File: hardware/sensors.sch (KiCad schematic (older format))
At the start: 31 parts, among them U1 LM358, U2 LAH-100P, U3 LOC110, U4 MCP6001, U5 ADA4805-1

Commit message: Draft layout of controller section
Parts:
- removed TH1, TH2: NXRT15WB473FA1B, symbol THERMISTOR
- added C73: 100n, Capacitors_SMD:C_0603, symbol C
- added C78: 1u, Capacitors_SMD:C_0603, symbol C
- added P13: CONN_01X02_MTMP, 2kwMotorController:TERM_2P_2-5_1990009, symbol CONN_01X02
- added P14: CONN_01X02_BTMP, 2kwMotorController:TERM_2P_2-5_1990009, symbol CONN_01X02
- R3: footprint Resistors_SMD:R_0603 -> Resistors_SMD:R_1206
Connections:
- wire segments 90 -> 94
- no-connect marks 0 -> 2
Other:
- note added: "NTC THERMISTOR\nPROBE OFF-BOARD:\nNXRT15WB473FA1B"
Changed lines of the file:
@@
 F 0 "R3" V 3180 2000 50  0000 C CNN
 F 1 "59.0" V 3100 2000 50  0000 C CNN
-F 2 "Resistors_SMD:R_0603" V 3030 2000 50  0001 C CNN
+F 2 "Resistors_SMD:R_1206" V 3030 2000 50  0001 C CNN
 F 3 "" H 3100 2000 50  0000 C CNN
 	1    3100 2000
@@
 L +12V #PWR04
 U 1 1 59A9BD78
-P 800 1550
-F 0 "#PWR04" H 800 1400 50  0001 C CNN
-F 1 "+12V" H 800 1690 50  0000 C CNN
-F 2 "" H 800 1550 50  0000 C CNN
-F 3 "" H 800 1550 50  0000 C CNN
-	1    800  1550
+P 950 1550
+F 0 "#PWR04" H 950 1400 50  0001 C CNN
+F 1 "+12V" H 950 1690 50  0000 C CNN
+F 2 "" H 950 1550 50  0000 C CNN
+F 3 "" H 950 1550 50  0000 C CNN
+	1    950  1550
 	1    0    0    -1
 $EndComp
@@
 L -12V #PWR2
 U 1 1 59A9BF35
-P 800 1750
-F 0 "#PWR2" H 800 1850 50  0001 C CNN
-F 1 "-12V" H 800 1900 50  0000 C CNN
-F 2 "" H 800 1750 50  0000 C CNN
-F 3 "" H 800 1750 50  0000 C CNN
-	1    800  1750
+P 950 2050
+F 0 "#PWR2" H 950 2150 50  0001 C CNN
+F 1 "-12V" H 950 2200 50  0000 C CNN
+F 2 "" H 950 2050 50  0000 C CNN
+F 3 "" H 950 2050 50  0000 C CNN
+	1    950  2050
 	-1   0    0    1
 $EndComp
@@
 	1650 1450 1600 1450
 Wire Wire Line
-	800  1600 1650 1600
-Wire Wire Line
-	800  1700 1650 1700
+	950  1600 1650 1600
 Wire Wire Line
 	2650 1650 3100 1650
@@
 Connection ~ 3500 6750
 Wire Wire Line
-	800  1600 800  1550
-Wire Wire Line
-	800  1750 800  1700
+	950  1550 950  1650
 Wire Wire Line
 	2650 1450 2700 1450
@@
 Connection ~ 5000 6650
 $Comp
-L THERMISTOR TH1
-U 1 1 59BEC427
-P 8300 2400
-F 0 "TH1" V 8400 2450 50  0000 C CNN
-F 1 "NXRT15WB473FA1B" V 8200 2400 50  0000 C BNN
-F 2 "" H 8300 2400 50  0001 C CNN
-F 3 "" H 8300 2400 50  0000 C CNN
-	1    8300 2400
-	1    0    0    -1
-$EndComp
-$Comp
 L R R38
 U 1 1 59BEC59E
@@
 $EndComp
 Wire Wire Line
-	8300 2700 8300 2650
-Wire Wire Line
-	8300 2050 8300 2150
+	8300 2450 8300 2700
+Wire Wire Line
+	8300 2050 8300 2350
 Wire Wire Line
 	8300 1750 8300 1650
@@
 $EndComp
 $Comp
-L THERMISTOR TH2
-U 1 1 59C18B62
-P 8300 4850
-F 0 "TH2" V 8400 4900 50  0000 C CNN
-F 1 "NXRT15WB473FA1B" V 8200 4850 50  0000 C BNN
-F 2 "" H 8300 4850 50  0001 C CNN
-F 3 "" H 8300 4850 50  0000 C CNN
-	1    8300 4850
-	1    0    0    -1
-$EndComp
-$Comp
 L R R59
 U 1 1 59C18B68
@@
 $EndComp
 Wire Wire Line
-	8300 5150 8300 5100
-Wire Wire Line
-	8300 4500 8300 4600
+	8300 4900 8300 5150
+Wire Wire Line
+	8300 4500 8300 4800
 Wire Wire Line
 	8300 4200 8300 4100
@@
 Connection ~ 2700 4650
 Connection ~ 2700 4250
+NoConn ~ 4100 1400
+NoConn ~ 4750 6050
+$Comp
+L C C73
+U 1 1 59CB7B98
+P 950 1800
+F 0 "C73" H 975 1900 50  0000 L CNN
+F 1 "100n" H 975 1700 50  0000 L CNN
+F 2 "Capacitors_SMD:C_0603" H 988 1650 50  0001 C CNN
+F 3 "" H 950 1800 50  0000 C CNN
+	1    950  1800
+	1    0    0    -1
+$EndComp
+Connection ~ 950  1600
+Wire Wire Line
+	950  1950 950  2050
+Wire Wire Line
+	950  2000 1550 2000
+Wire Wire Line
+	1550 2000 1550 1700
+Wire Wire Line
+	1550 1700 1650 1700
+Connection ~ 950  2000
+$Comp
+L C C78
+U 1 1 59CB93D8
+P 1250 1800
+F 0 "C78" H 1275 1900 50  0000 L CNN
+F 1 "1u" H 1275 1700 50  0000 L CNN
+F 2 "Capacitors_SMD:C_0603" H 1288 1650 50  0001 C CNN
+F 3 "" H 1250 1800 50  0000 C CNN
+	1    1250 1800
+	1    0    0    -1
+$EndComp
+Wire Wire Line
+	1250 1650 1250 1600
+Connection ~ 1250 1600
+Wire Wire Line
+	1250 1950 1250 2000
+Connection ~ 1250 2000
+$Comp
+L CONN_01X02 P13
+U 1 1 59CD3AE3
+P 8100 2400
+F 0 "P13" H 8100 2550 50  0000 C CNN
+F 1 "CONN_01X02_MTMP" V 8200 2400 50  0000 C CNN
+F 2 "2kwMotorController:TERM_2P_2-5_1990009" H 8100 2400 50  0001 C CNN
+F 3 "" H 8100 2400 50  0000 C CNN
+	1    8100 2400
+	-1   0    0    1
+$EndComp
+Text Notes 7000 2500 0    60   ~ 0
+NTC THERMISTOR\nPROBE OFF-BOARD:\nNXRT15WB473FA1B
+Text Notes 7000 5000 0    60   ~ 0
+NTC THERMISTOR\nPROBE OFF-BOARD:\nNXRT15WB473FA1B
+$Comp
+L CONN_01X02 P14
+U 1 1 59CD58D2
+P 8100 4850
+F 0 "P14" H 8100 5000 50  0000 C CNN
+F 1 "CONN_01X02_BTMP" V 8200 4850 50  0000 C CNN
+F 2 "2kwMotorController:TERM_2P_2-5_1990009" H 8100 4850 50  0001 C CNN
+F 3 "" H 8100 4850 50  0000 C CNN
+	1    8100 4850
+	-1   0    0    1
+$EndComp
 $EndSCHEMATC

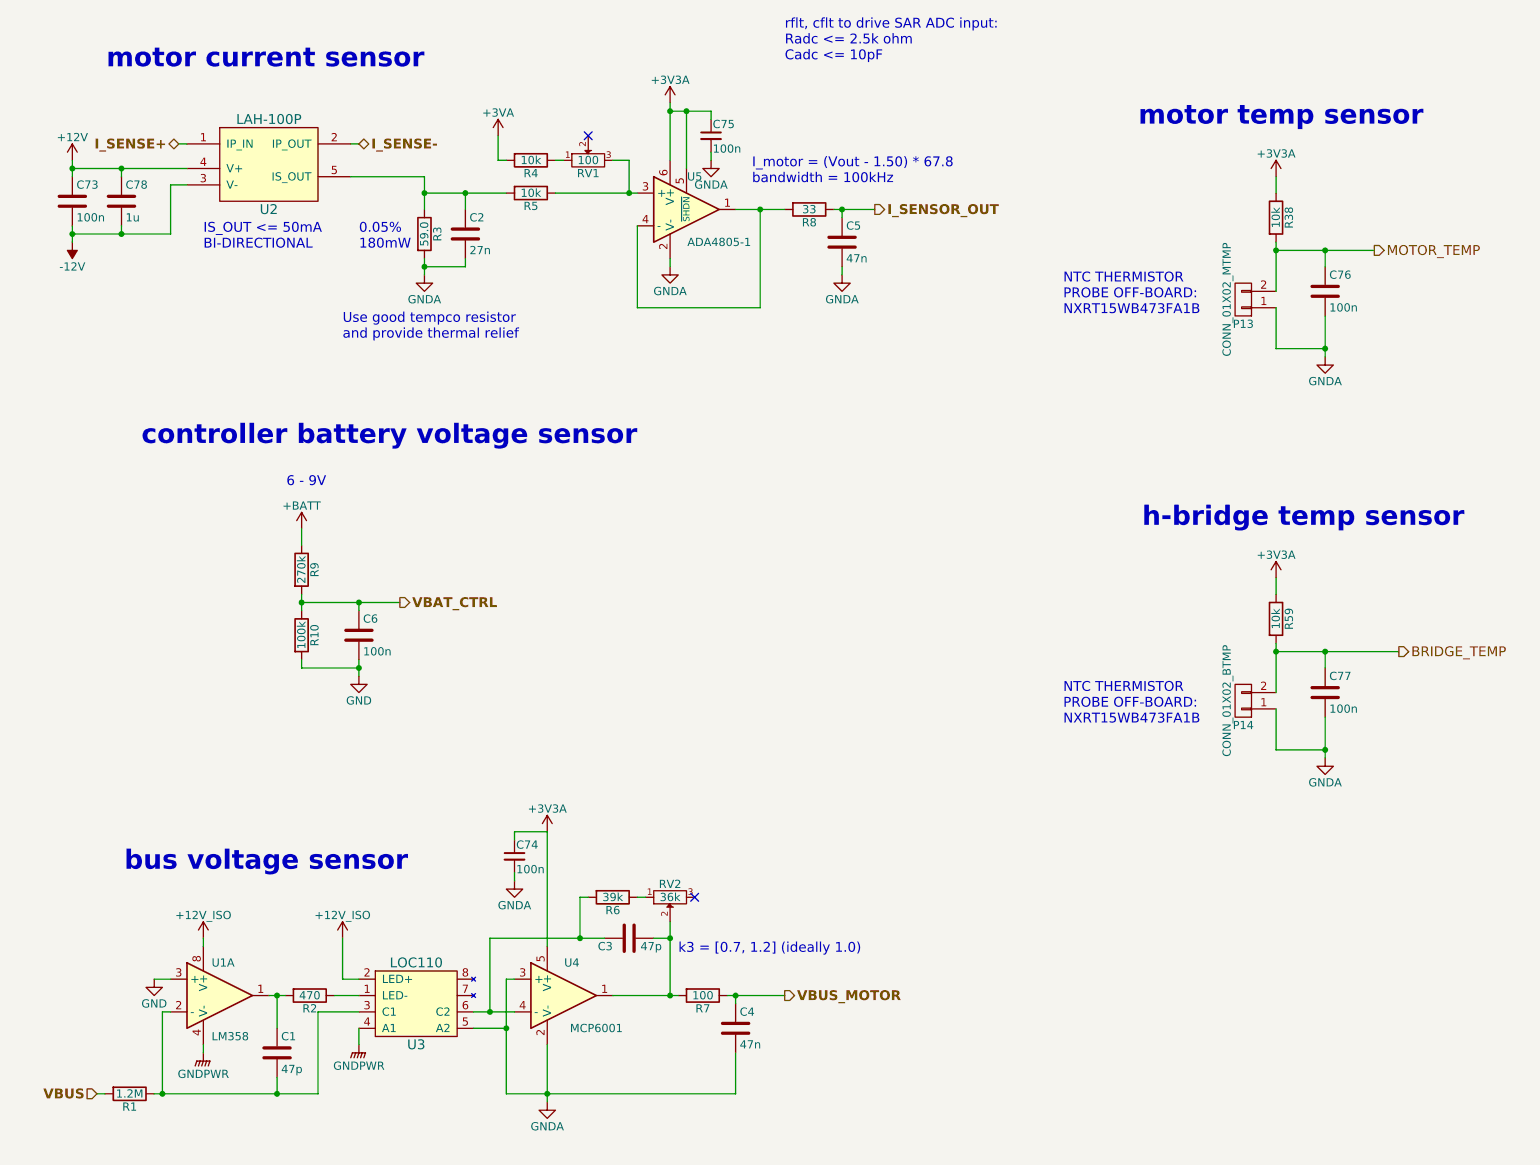
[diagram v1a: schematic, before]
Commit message: Gate driver layout mostly complete
- Gate driver layout
- Switch LM5102 for UCC27211 (higher current, more robust)
- Tweak gate drive circuit passives
- No soldermask on high-current traces
- Fix error in orientation of LAH-100P footprint
- Improved draft layout of control section
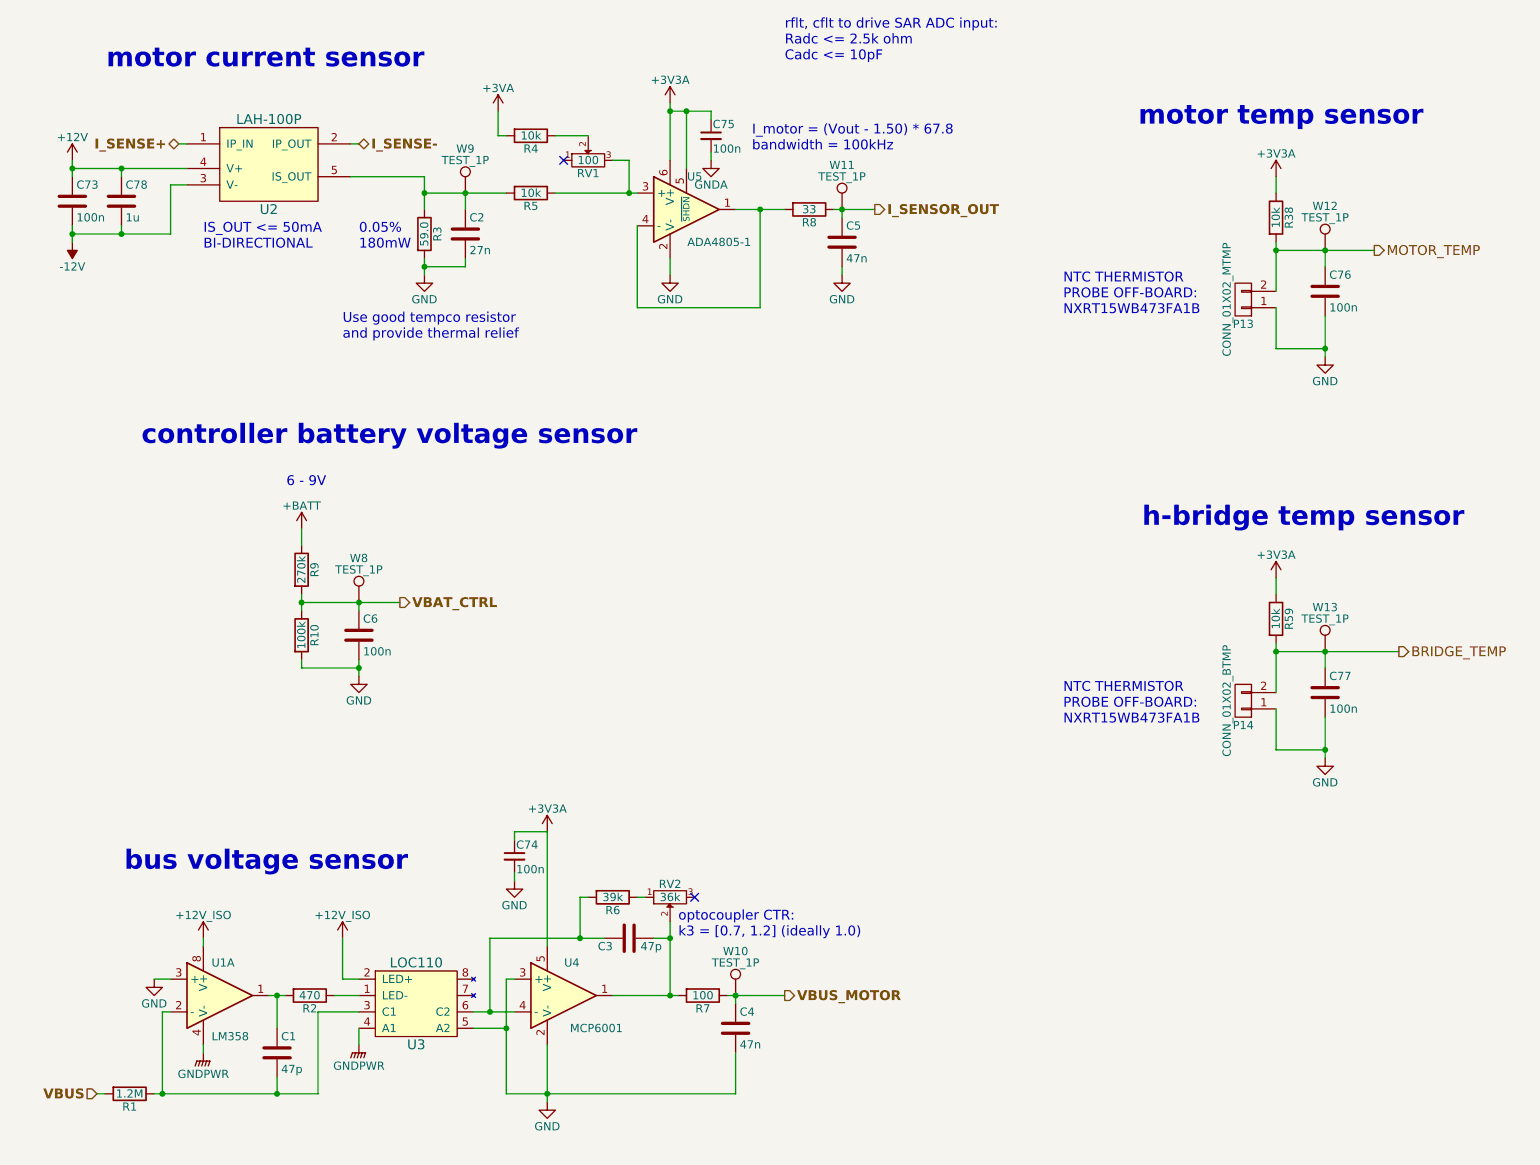
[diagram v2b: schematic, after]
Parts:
- added W10, W11, W12, W13, W8, W9: TEST_1P, symbol TEST_1P
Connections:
- net BRIDGE_TEMP: now also W13.1
- net GND: now also C2.2, C4.2, C5.2, C74.2, C76.2, C77.2, P13.1 (P1), P14.1 (P1), R3.2, U3.5 (A2), U4.2 (V-), U4.3 (+), U5.2 (V-)
- net GNDA: no longer C2.2, C4.2, C5.2, C74.2, C76.2, C77.2, P13.1 (P1), P14.1 (P1), R3.2, U3.5 (A2), U4.2 (V-), U4.3 (+), U5.2 (V-)
- net I_SENSOR_OUT: now also W11.1
- net MOTOR_TEMP: now also W12.1
- net VBAT_CTRL: now also W8.1
- net VBUS_MOTOR: now also W10.1
- net at C2.1, R3.1, R5.2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: now also W9.1
- net at R4.1: now also RV1.2; no longer RV1.1
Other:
- note added: "optocoupler CTR:\nk3 = [0.7, 1.2] (ideally 1.0)"
- note removed: "k3 = [0.7, 1.2] (ideally 1.0)"
- moved on the sheet: R4
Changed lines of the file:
@@
 L R R4
 U 1 1 5975CA28
-P 3750 1550
-F 0 "R4" V 3830 1550 50  0000 C CNN
-F 1 "10k" V 3750 1550 50  0000 C CNN
-F 2 "Resistors_SMD:R_0603" V 3680 1550 50  0001 C CNN
-F 3 "" H 3750 1550 50  0000 C CNN
-	1    3750 1550
+P 3750 1400
+F 0 "R4" V 3830 1400 50  0000 C CNN
+F 1 "10k" V 3750 1400 50  0000 C CNN
+F 2 "Resistors_SMD:R_0603" V 3680 1400 50  0001 C CNN
+F 3 "" H 3750 1400 50  0000 C CNN
+	1    3750 1400
 	0    1    1    0
 $EndComp
@@
 Connection ~ 3100 1750
 Wire Wire Line
-	4600 2150 4600 2200
+	4600 2150 4600 2250
 Wire Wire Line
 	4400 1950 4400 2450
@@
 	4600 1200 4600 1550
 Wire Wire Line
-	3550 1400 3550 1550
-Wire Wire Line
-	3550 1550 3600 1550
+	3550 1250 3550 1400
+Wire Wire Line
+	3550 1400 3600 1400
 Wire Wire Line
 	4350 1550 4350 1750
@@
 	2650 1450 2700 1450
 Connection ~ 3600 6850
-Text Notes 4650 6400 0    60   ~ 0
-k3 = [0.7, 1.2] (ideally 1.0)
+Text Notes 4650 6300 0    60   ~ 0
+optocoupler CTR:\nk3 = [0.7, 1.2] (ideally 1.0)
 $Comp
 L POT RV2
@@
 Connection ~ 4600 6650
 Wire Wire Line
-	3900 1550 3950 1550
+	3900 1400 4100 1400
 Wire Wire Line
 	4250 1550 4350 1550
@@
 Text Notes 5300 950  0    60   ~ 0
 rflt, cflt to drive SAR ADC input:\nRadc <= 2.5k ohm\nCadc <= 10pF
-Text Notes 5100 1700 0    60   ~ 0
+Text Notes 5100 1500 0    60   ~ 0
 I_motor = (Vout - 1.50) * 67.8\nbandwidth = 100kHz
 Text Notes 2700 2100 0    60   ~ 0
@@
 L +3VA #PWR05
 U 1 1 59C015DC
-P 3550 1400
-F 0 "#PWR05" H 3550 1250 50  0001 C CNN
-F 1 "+3VA" H 3550 1540 50  0000 C CNN
-F 2 "" H 3550 1400 50  0000 C CNN
-F 3 "" H 3550 1400 50  0000 C CNN
-	1    3550 1400
+P 3550 1250
+F 0 "#PWR05" H 3550 1100 50  0001 C CNN
+F 1 "+3VA" H 3550 1390 50  0000 C CNN
+F 2 "" H 3550 1250 50  0000 C CNN
+F 3 "" H 3550 1250 50  0000 C CNN
+	1    3550 1250
 	1    0    0    -1
 $EndComp
@@
 	4850 1550 4850 1500
 Connection ~ 4700 1250
-$Comp
-L GNDA #PWR014
-U 1 1 59BFC0AB
-P 3100 2250
-F 0 "#PWR014" H 3100 2000 50  0001 C CNN
-F 1 "GNDA" H 3100 2100 50  0000 C CNN
-F 2 "" H 3100 2250 50  0000 C CNN
-F 3 "" H 3100 2250 50  0000 C CNN
-	1    3100 2250
-	1    0    0    -1
-$EndComp
-$Comp
-L GNDA #PWR015
-U 1 1 59BFC11D
-P 4600 2200
-F 0 "#PWR015" H 4600 1950 50  0001 C CNN
-F 1 "GNDA" H 4600 2050 50  0000 C CNN
-F 2 "" H 4600 2200 50  0000 C CNN
-F 3 "" H 4600 2200 50  0000 C CNN
-	1    4600 2200
-	1    0    0    -1
-$EndComp
-$Comp
-L GNDA #PWR016
-U 1 1 59BFC369
-P 5650 2250
-F 0 "#PWR016" H 5650 2000 50  0001 C CNN
-F 1 "GNDA" H 5650 2100 50  0000 C CNN
-F 2 "" H 5650 2250 50  0000 C CNN
-F 3 "" H 5650 2250 50  0000 C CNN
-	1    5650 2250
-	1    0    0    -1
-$EndComp
 Wire Wire Line
 	4850 1250 4850 1300
@@
 	3600 7250 5000 7250
 Connection ~ 3850 7250
-$Comp
-L GNDA #PWR017
-U 1 1 59BFDFDA
-P 3850 7300
-F 0 "#PWR017" H 3850 7050 50  0001 C CNN
-F 1 "GNDA" H 3850 7150 50  0000 C CNN
-F 2 "" H 3850 7300 50  0000 C CNN
-F 3 "" H 3850 7300 50  0000 C CNN
-	1    3850 7300
-	1    0    0    -1
-$EndComp
 Wire Wire Line
 	3650 5650 3850 5650
@@
 Wire Wire Line
 	3650 5700 3650 5650
-$Comp
-L GNDA #PWR018
-U 1 1 59C06560
-P 3650 5950
-F 0 "#PWR018" H 3650 5700 50  0001 C CNN
-F 1 "GNDA" H 3650 5800 50  0000 C CNN
-F 2 "" H 3650 5950 50  0000 C CNN
-F 3 "" H 3650 5950 50  0000 C CNN
-	1    3650 5950
-	1    0    0    -1
-$EndComp
 Wire Wire Line
 	3650 5950 3650 5900
 Wire Wire Line
 	4050 6050 4100 6050
-$Comp
-L GNDA #PWR019
-U 1 1 59C10F8D
-P 8600 2750
-F 0 "#PWR019" H 8600 2500 50  0001 C CNN
-F 1 "GNDA" H 8600 2600 50  0000 C CNN
-F 2 "" H 8600 2750 50  0000 C CNN
-F 3 "" H 8600 2750 50  0000 C CNN
-	1    8600 2750
-	1    0    0    -1
-$EndComp
 $Comp
 L R R59
@@
 	8600 4950 8600 5200
 $Comp
-L +3V3A #PWR020
+L +3V3A #PWR014
 U 1 1 59C18B81
 P 8300 4100
-F 0 "#PWR020" H 8300 3950 50  0001 C CNN
+F 0 "#PWR014" H 8300 3950 50  0001 C CNN
 F 1 "+3V3A" H 8300 4240 50  0000 C CNN
 F 2 "" H 8300 4100 50  0000 C CNN
@@
 Connection ~ 8600 4550
 Connection ~ 8600 5150
-$Comp
-L GNDA #PWR021
-U 1 1 59C18BA9
-P 8600 5200
-F 0 "#PWR021" H 8600 4950 50  0001 C CNN
-F 1 "GNDA" H 8600 5050 50  0000 C CNN
-F 2 "" H 8600 5200 50  0000 C CNN
-F 3 "" H 8600 5200 50  0000 C CNN
-	1    8600 5200
-	1    0    0    -1
-$EndComp
 Wire Wire Line
 	8300 2700 8600 2700
@@
 Connection ~ 2700 4650
 Connection ~ 2700 4250
-NoConn ~ 4100 1400
 NoConn ~ 4750 6050
 $Comp
@@
 	-1   0    0    1
 $EndComp
+NoConn ~ 3950 1550
+$Comp
+L GND #PWR015
+U 1 1 59C15774
+P 3850 7300
+F 0 "#PWR015" H 3850 7050 50  0001 C CNN
+F 1 "GND" H 3850 7150 50  0000 C CNN
+F 2 "" H 3850 7300 50  0000 C CNN
+F 3 "" H 3850 7300 50  0000 C CNN
+	1    3850 7300
+	1    0    0    -1
+$EndComp
+$Comp
+L GND #PWR016
+U 1 1 59C157E9
+P 8600 5200
+F 0 "#PWR016" H 8600 4950 50  0001 C CNN
+F 1 "GND" H 8600 5050 50  0000 C CNN
+F 2 "" H 8600 5200 50  0000 C CNN
+F 3 "" H 8600 5200 50  0000 C CNN
+	1    8600 5200
+	1    0    0    -1
+$EndComp
+$Comp
+L GND #PWR017
+U 1 1 59C15D06
+P 8600 2750
+F 0 "#PWR017" H 8600 2500 50  0001 C CNN
+F 1 "GND" H 8600 2600 50  0000 C CNN
+F 2 "" H 8600 2750 50  0000 C CNN
+F 3 "" H 8600 2750 50  0000 C CNN
+	1    8600 2750
+	1    0    0    -1
+$EndComp
+$Comp
+L GND #PWR018
+U 1 1 59C16167
+P 5650 2250
+F 0 "#PWR018" H 5650 2000 50  0001 C CNN
+F 1 "GND" H 5650 2100 50  0000 C CNN
+F 2 "" H 5650 2250 50  0000 C CNN
+F 3 "" H 5650 2250 50  0000 C CNN
+	1    5650 2250
+	1    0    0    -1
+$EndComp
+$Comp
+L GND #PWR019
+U 1 1 59C169DF
+P 4600 2250
+F 0 "#PWR019" H 4600 2000 50  0001 C CNN
+F 1 "GND" H 4600 2100 50  0000 C CNN
+F 2 "" H 4600 2250 50  0000 C CNN
+F 3 "" H 4600 2250 50  0000 C CNN
+	1    4600 2250
+	1    0    0    -1
+$EndComp
+$Comp
+L GND #PWR020
+U 1 1 59C16EAB
+P 3100 2250
+F 0 "#PWR020" H 3100 2000 50  0001 C CNN
+F 1 "GND" H 3100 2100 50  0000 C CNN
+F 2 "" H 3100 2250 50  0000 C CNN
+F 3 "" H 3100 2250 50  0000 C CNN
+	1    3100 2250
+	1    0    0    -1
+$EndComp
+$Comp
+L GND #PWR021
+U 1 1 59C17E29
+P 3650 5950
+F 0 "#PWR021" H 3650 5700 50  0001 C CNN
+F 1 "GND" H 3650 5800 50  0000 C CNN
+F 2 "" H 3650 5950 50  0000 C CNN
+F 3 "" H 3650 5950 50  0000 C CNN
+	1    3650 5950
+	1    0    0    -1
+$EndComp
+$Comp
+L TEST_1P W11
+U 1 1 59C1A0CE
+P 5650 1850
+F 0 "W11" H 5650 2120 50  0000 C CNN
+F 1 "TEST_1P" H 5650 2050 50  0000 C CNN
+F 2 "" H 5850 1850 50  0001 C CNN
+F 3 "" H 5850 1850 50  0000 C CNN
+	1    5650 1850
+	1    0    0    -1
+$EndComp
+$Comp
+L TEST_1P W12
+U 1 1 59C1B0A9
+P 8600 2100
+F 0 "W12" H 8600 2370 50  0000 C CNN
+F 1 "TEST_1P" H 8600 2300 50  0000 C CNN
+F 2 "" H 8800 2100 50  0001 C CNN
+F 3 "" H 8800 2100 50  0000 C CNN
+	1    8600 2100
+	1    0    0    -1
+$EndComp
+$Comp
+L TEST_1P W13
+U 1 1 59C1B7B3
+P 8600 4550
+F 0 "W13" H 8600 4820 50  0000 C CNN
+F 1 "TEST_1P" H 8600 4750 50  0000 C CNN
+F 2 "" H 8800 4550 50  0001 C CNN
+F 3 "" H 8800 4550 50  0000 C CNN
+	1    8600 4550
+	1    0    0    -1
+$EndComp
+$Comp
+L TEST_1P W10
+U 1 1 59C1BB65
+P 5000 6650
+F 0 "W10" H 5000 6920 50  0000 C CNN
+F 1 "TEST_1P" H 5000 6850 50  0000 C CNN
+F 2 "" H 5200 6650 50  0001 C CNN
+F 3 "" H 5200 6650 50  0000 C CNN
+	1    5000 6650
+	1    0    0    -1
+$EndComp
+$Comp
+L TEST_1P W8
+U 1 1 59C1D3A6
+P 2700 4250
+F 0 "W8" H 2700 4520 50  0000 C CNN
+F 1 "TEST_1P" H 2700 4450 50  0000 C CNN
+F 2 "" H 2900 4250 50  0001 C CNN
+F 3 "" H 2900 4250 50  0000 C CNN
+	1    2700 4250
+	1    0    0    -1
+$EndComp
+$Comp
+L TEST_1P W9
+U 1 1 59C1EA64
+P 3350 1750
+F 0 "W9" H 3350 2020 50  0000 C CNN
+F 1 "TEST_1P" H 3350 1950 50  0000 C CNN
+F 2 "" H 3550 1750 50  0001 C CNN
+F 3 "" H 3550 1750 50  0000 C CNN
+	1    3350 1750
+	1    0    0    -1
+$EndComp
 $EndSCHEMATC

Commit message: All routing finished
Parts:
- added R44: 18k, Resistors_SMD:R_0603, symbol R
- added R45: 2k, Resistors_SMD:R_0603, symbol R
- added unit 2 of U1
- C1, C3: value 47p -> 10p
- C4: value 47n -> 100n
- R1: value 1.2M -> 120k
- R7: value 100 -> 47
- U1: value LM358 -> LM358A; footprint SMD_Packages:SOIC-8-N -> Housings_SOIC:SOIC-8_3.9x4.9mm_Pitch1.27mm
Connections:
- net +12V_ISO: now also U1.8 (V+)
- net GND: no longer U1.3 (+)
- net GNDPWR: now also R45.2, U1.4 (V-), U1.5 (+)
- net VBUS: now also R44.1; no longer R1.2
- net at C1.1, R2.2: now also U1.7; no longer U1.1
- net at C1.2, R1.1, U3.3 (C1): now also U1.6 (-); no longer U1.2 (-)
- new net: R1.2, U1.1, U1.2 (-)
- new net: R44.2, R45.1, U1.3 (+)
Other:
- moved on the sheet: C1, C3, C4, C74, R1, R2, R6, R7, RV2, U3, U4, W10

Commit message: All DRC/ERC passed
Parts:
- removed W10, W11, W12, W13, W8, W9: TEST_1P, symbol TEST_1P
- added TP1, TP2, TP3, TP4, TP5, TP6, TP7, TP8: TEST_POINT, 2kwMotorController:TEST_PAD_1.27mm, symbol TEST_POINT
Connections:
- net GNDA is gone; now on net GND: C75.2
- net BRIDGE_TEMP: now also TP8.1
- net I_SENSOR_OUT: now also TP5.1
- net MOTOR_TEMP: now also TP7.1
- net VBAT_CTRL: now also TP2.1
- net VBUS_MOTOR: now also TP6.1
- net ISENSE_OUT: now reaches C2.1, R3.1, R5.2, U2.5 (IS_OUT)
- net ISENSE_OUT: now also TP3.1
- net IS_SUM: now reaches R5.1, RV1.3, U5.3 (+)
- net IS_SUM: now also TP4.1
- net VBUS_DIV: now reaches R1.2, U1.1, U1.2 (-)
- net VBUS_DIV: now also TP1.1
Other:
- moved on the sheet: C1, C3, C4, C74, R1, R2, R6, R7, RV2, U1B, U3, U4
